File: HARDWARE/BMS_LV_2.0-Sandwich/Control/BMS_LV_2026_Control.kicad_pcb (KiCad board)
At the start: 6 copper layers, 62.5 x 40.8 mm, 89 parts, among them IC1 TAR5S33UTE85LF, IC2 TAR5S33UTE85LF, IC4 TPS54202HDDCR, J1 Conn_01x26, J6 Conn_01x09_Female, U1 STM32G484RETx, U7 ADM3057ExRW, Y1 ATX-11-F-32.000MHZ-F05-T

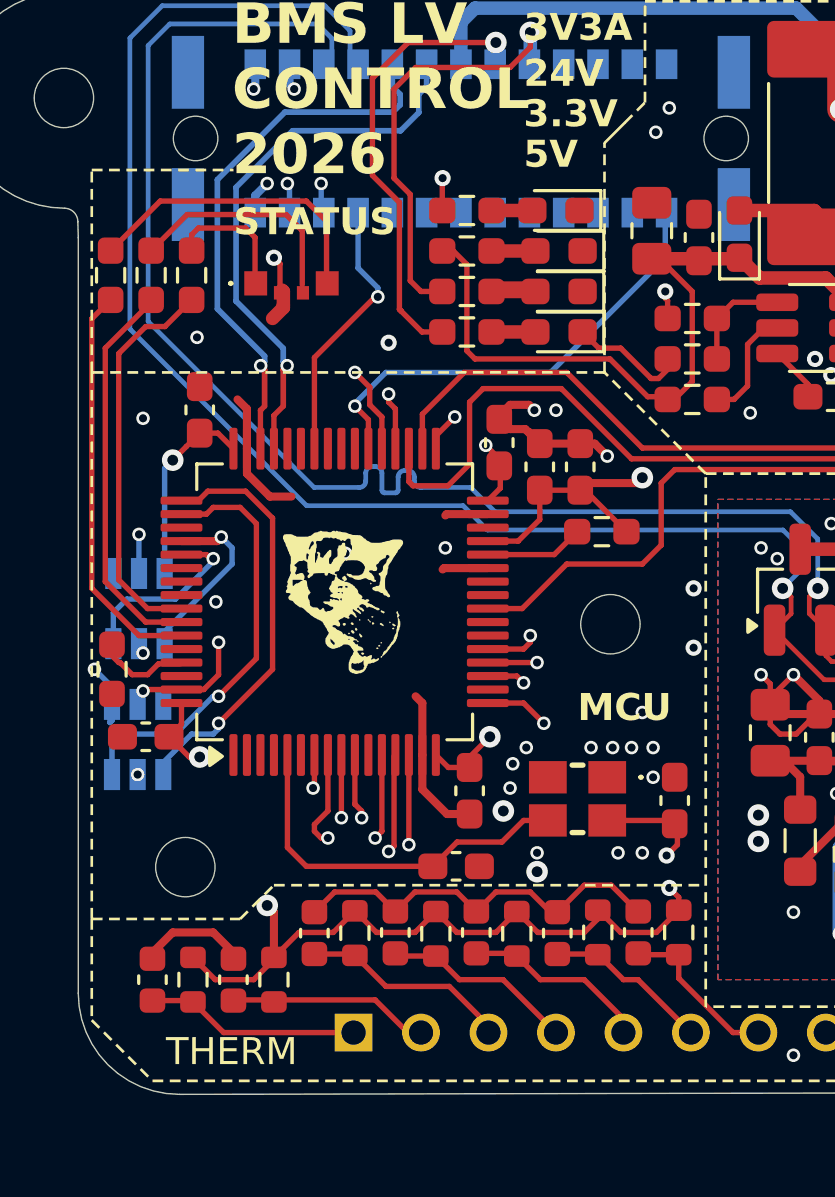
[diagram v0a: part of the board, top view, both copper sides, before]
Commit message: Naprawiono: załączanie lv, brak zlącza programatora (XD) oraz brak podłączenia czujnika prądu :9
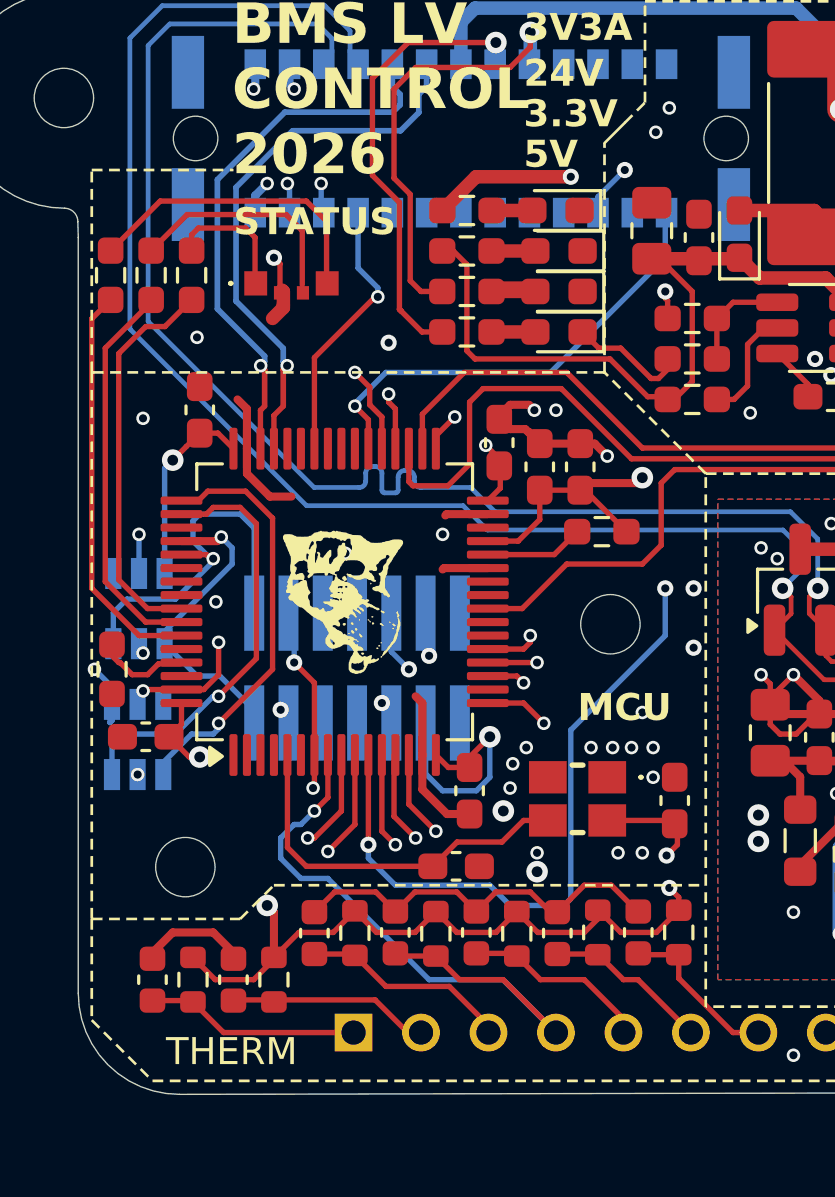
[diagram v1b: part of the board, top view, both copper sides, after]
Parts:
- added J3: FTSH-107-01-L-D-K, Footprint:FTSH-107-XX-YYY-DV-K, B.Cu at (152.3, 105.0)
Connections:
- J1 pad 11: unconnected-(J1-Pin_11-Pad11) -> /CurrentSensor_Out
- U1 pad 11: unconnected-(U1-PC3-Pad11) -> /CurrentSensor_Out
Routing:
- net /CurrentSensor_Out: track 0.00 -> 50.6 mm, vias 0 -> 3
- net /Control/SWDIO: track 14.5 -> 27.0 mm, vias 1 -> 2
- net /Control/SWCLK: track 15.9 -> 25.7 mm, vias 1 -> 2
- net /Control/URAT_TX: track 6.97 -> 14.5 mm
- net /3V3: track 44.7 -> 50.9 mm
- net /Therm_6: track 28.1 -> 33.7 mm
- net /Control/NRST: track 15.3 -> 20.7 mm, vias 2 -> 3
- net /Control/URAT_RX: track 6.24 -> 10.6 mm
- net /Therm_4: track 28.4 -> 24.6 mm
- net /3V3A: track 130.2 -> 131.6 mm
- net /Therm_3: track 20.5 -> 21.4 mm
- net /Therm_2: track 18.5 -> 19.0 mm
- net GND: vias 61 -> 63

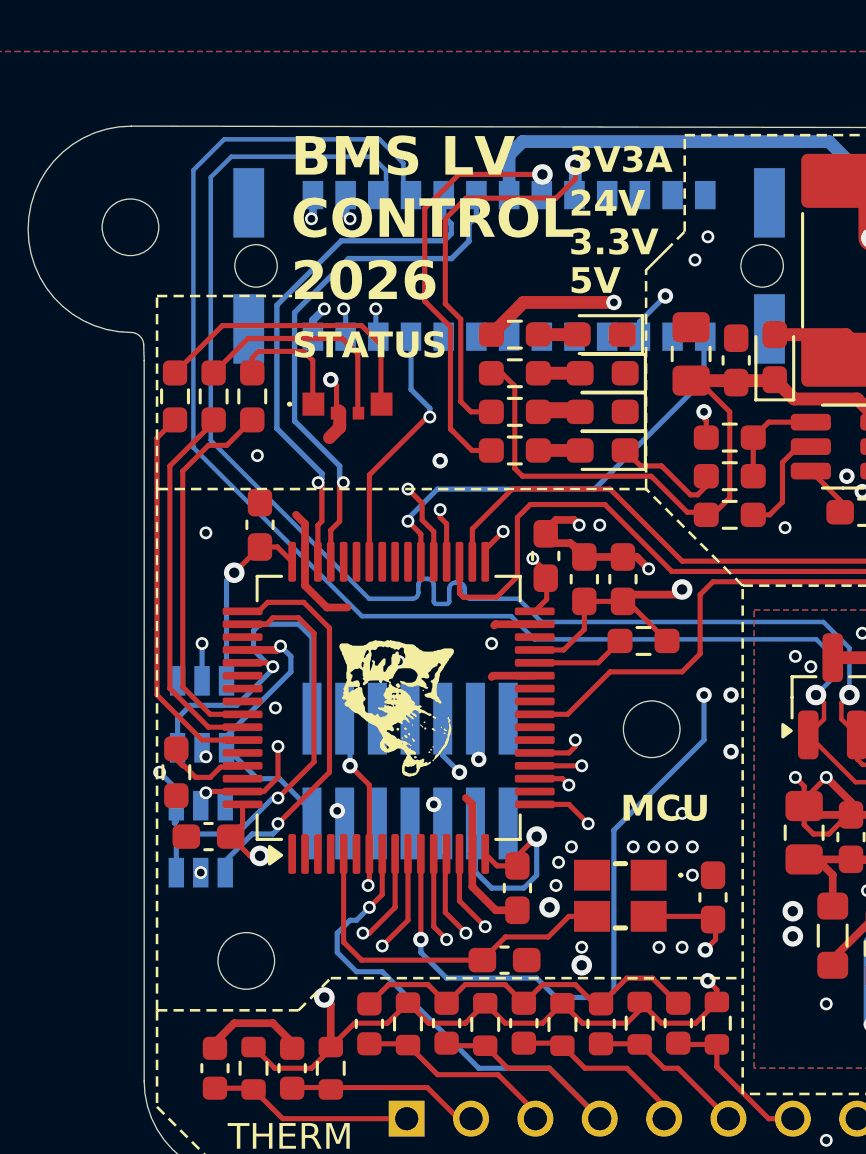
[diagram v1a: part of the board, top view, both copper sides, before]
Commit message: Zmieniono ledy, przesunięto pomiar napięcia z czujnika prądu na adc2
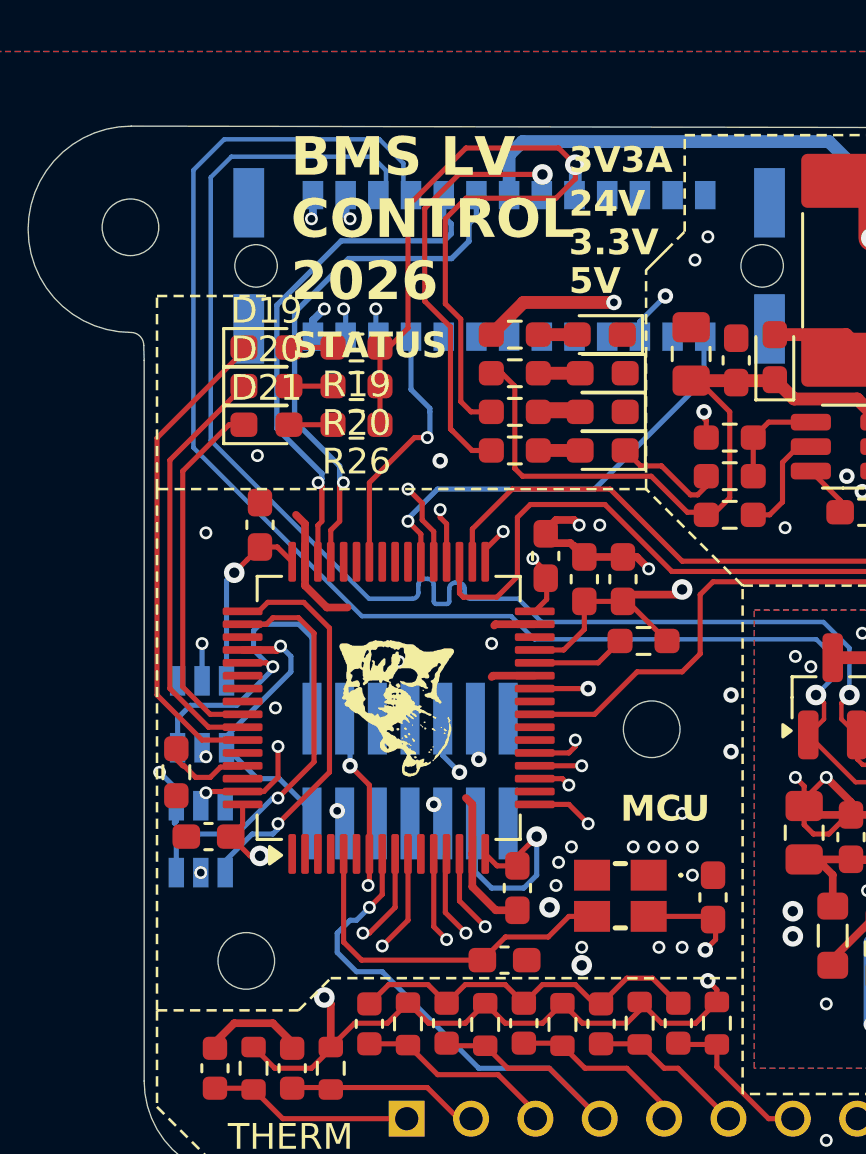
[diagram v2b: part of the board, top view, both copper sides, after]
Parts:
- removed D2: LED_BKGR, Footprint:APFA2507LSURKSYKZGKC
- added D19: ~, LED_SMD:LED_0603_1608Metric_Pad1.05x0.95mm_HandSolder, F.Cu at (146.8, 88.5)
- added D20: ~, LED_SMD:LED_0603_1608Metric_Pad1.05x0.95mm_HandSolder, F.Cu at (146.8, 90.0)
- added D21: ~, LED_SMD:LED_0603_1608Metric_Pad1.05x0.95mm_HandSolder, F.Cu at (146.8, 91.5)
- R19, R20, R26: value 750R -> 100
- moved R20 7.06 mm to (150.2, 90.0), turned to 180 degrees
- moved R19 5.87 mm to (150.2, 88.5), turned to 180 degrees
- moved R26 4.20 mm to (150.2, 91.5), turned to 180 degrees
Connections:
- R19 pad 1: Net-(D2-GA) -> /3V3
- R19 pad 2: /Control/GREEN -> Net-(D19-A)
- R20 pad 1: Net-(D2-RA) -> /3V3
- R20 pad 2: /Control/YELLOW -> Net-(D20-A)
- R26 pad 1: Net-(D2-BA) -> /3V3
- R26 pad 2: /Control/RED -> Net-(D21-A)
- U1 pad 11: /CurrentSensor_Out -> unconnected-(U1-PC3-Pad11)
- U1 pad 26: unconnected-(U1-PB2-Pad26) -> /CurrentSensor_Out
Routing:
- net /CurrentSensor_Out: track 50.6 -> 26.7 mm, vias 3 -> 2
- net /3V3: track 50.9 -> 67.8 mm
- net Net-(D2-RA): track 11.1 -> 0.00 mm
- net Net-(D2-GA): track 8.40 -> 0.00 mm
- net Net-(D2-BA): track 4.59 -> 0.00 mm
- net /Control/YELLOW: track 15.0 -> 18.9 mm
- net GND: track 65.2 -> 62.5 mm, vias 63 -> 62
- net /Control/GREEN: track 14.5 -> 16.4 mm
- net Net-(D21-A): track 0.00 -> 1.71 mm
- net Net-(D20-A): track 0.00 -> 1.71 mm
- net Net-(D19-A): track 0.00 -> 1.71 mm

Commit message: Poprawki , tvs , programator
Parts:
- D7, D8: footprint Footprint:SOT95P285X140-6N -> Footprint:SOT65P210X110-6N
- moved D7 1.05 mm to (144.8, 108.5), turned to 0 degrees
- moved D8 0.74 mm to (144.9, 103.0), turned to 0 degrees
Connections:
- D7 pad 5: GND -> /3V3
- D8 pad 4: /Control/URAT_RX -> /Control/URAT_TX
- D8 pad 5: GND -> /3V3
- D8 pad 6: /Control/URAT_TX -> /Control/URAT_RX
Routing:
- net /Control/SWCLK: track 25.7 -> 34.0 mm, vias 2 -> 4
- net /Control/URAT_TX: track 14.5 -> 7.48 mm
- net /3V3: track 67.8 -> 73.6 mm, vias 8 -> 11
- net /Control/NRST: track 20.7 -> 24.1 mm
- net GND: track 62.5 -> 64.8 mm, vias 62 -> 57
- net /Control/URAT_RX: track 10.6 -> 12.7 mm
- net /Control/SWDIO: track 27.0 -> 28.5 mm, vias 2 -> 3

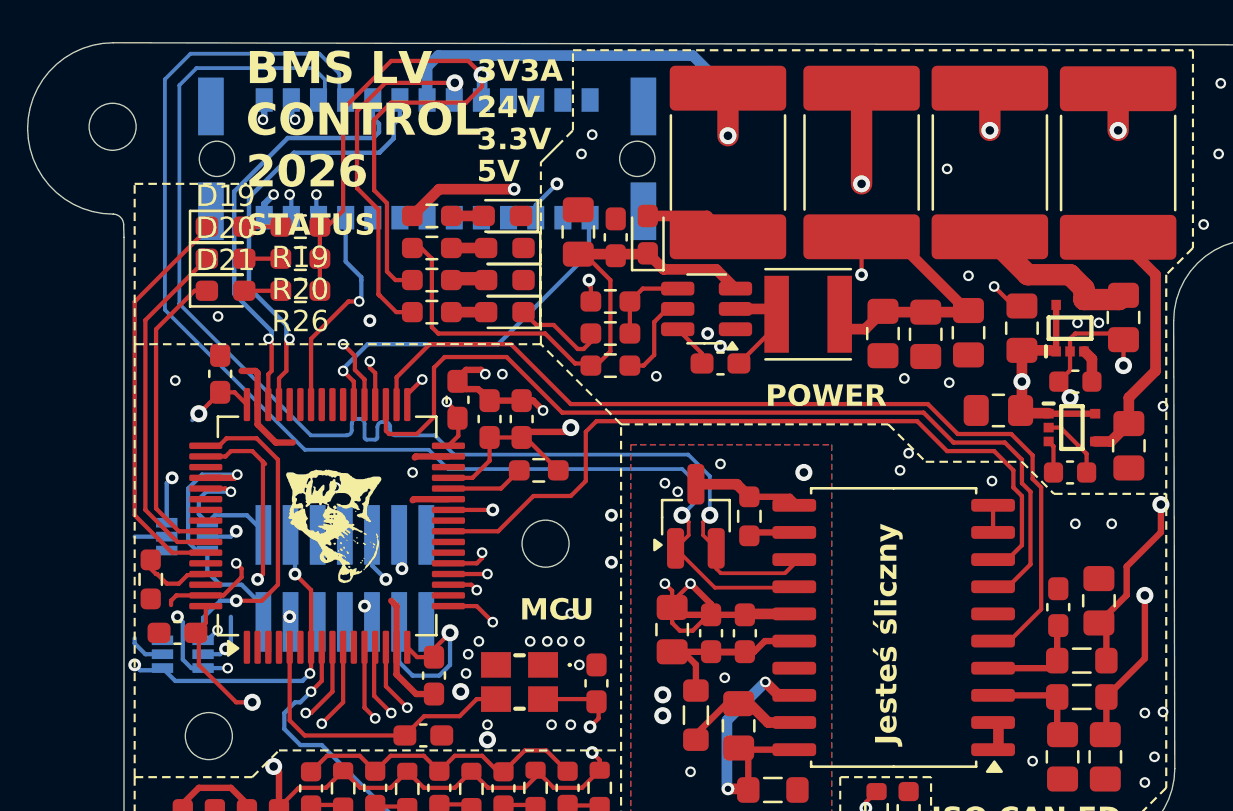
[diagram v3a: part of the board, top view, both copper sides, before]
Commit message: Zmieniono złącze programatora na kątowe
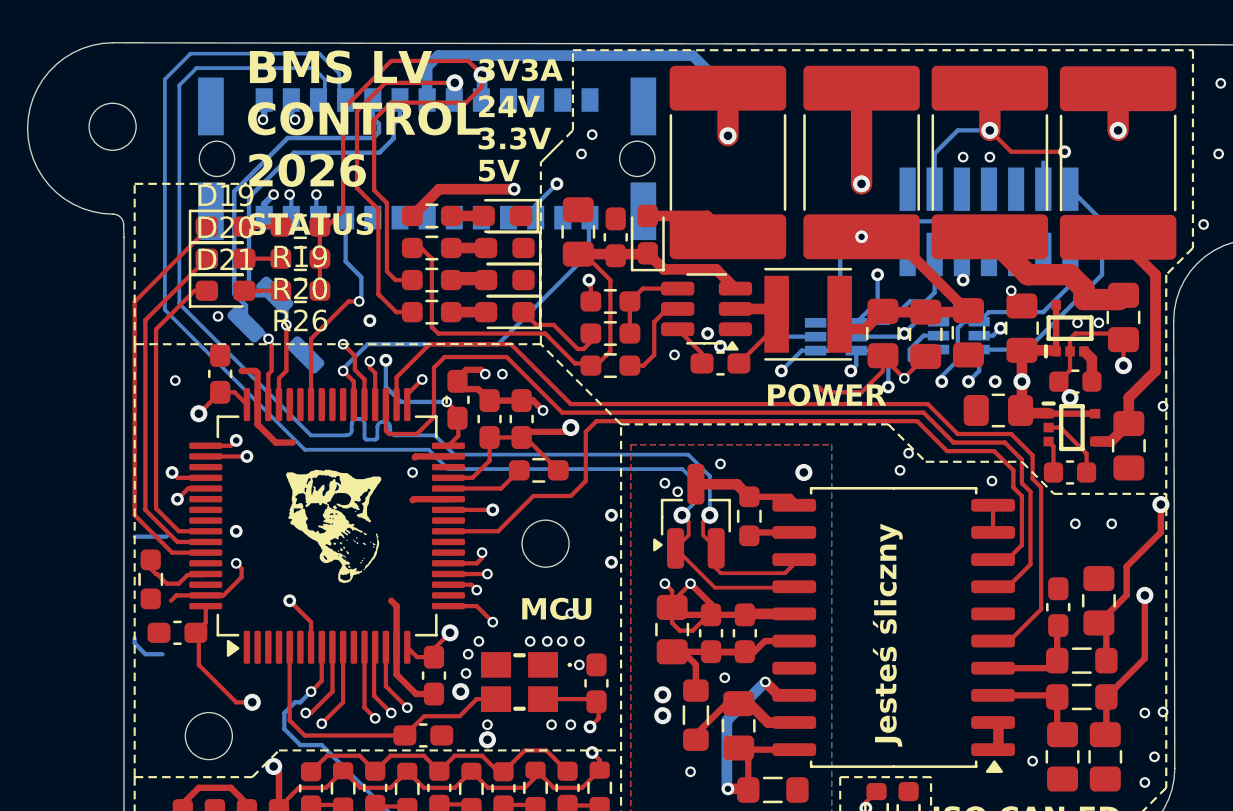
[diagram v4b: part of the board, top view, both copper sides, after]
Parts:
- added D10: D_TVS_Dual_AAC, Package_TO_SOT_SMD:SOT-23_Handsoldering, B.Cu at (149.4, 93.4)
- J3: footprint Footprint:FTSH-107-XX-YYY-DV-K -> Footprint:FTSH-107-XX-YYY-DH-TR
- moved D8 37.3 mm to (181.1, 93.6)
- moved J3 34.4 mm to (182.5, 88.3)
- moved D7 34.0 mm to (175.3, 93.7)
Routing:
- net /Control/URAT_RX: track 12.7 -> 71.2 mm, vias 1 -> 2
- net /Control/URAT_TX: track 7.48 -> 66.0 mm, vias 1 -> 2
- net /Control/NRST: track 24.1 -> 61.5 mm, vias 3 -> 2
- net /Control/SWCLK: track 34.0 -> 56.8 mm
- net /3V3: track 73.6 -> 92.4 mm, vias 11 -> 13
- net /Control/SWDIO: track 28.5 -> 46.8 mm, vias 3 -> 2
- net GND: track 64.8 -> 76.4 mm, vias 57 -> 55
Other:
- board text added: "BMS SANDWICH 2026 By Wiktor Krakowski V1.1"
- board text removed: "BMS SANDWICH 2026 By Wiktor Krakowski V1.0"
